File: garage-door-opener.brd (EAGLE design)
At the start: 54.3 x 47 mm, 17 parts, among them IC1 LM2575-3.3T, K1 RR1A, T1 BC547, X2 Connector

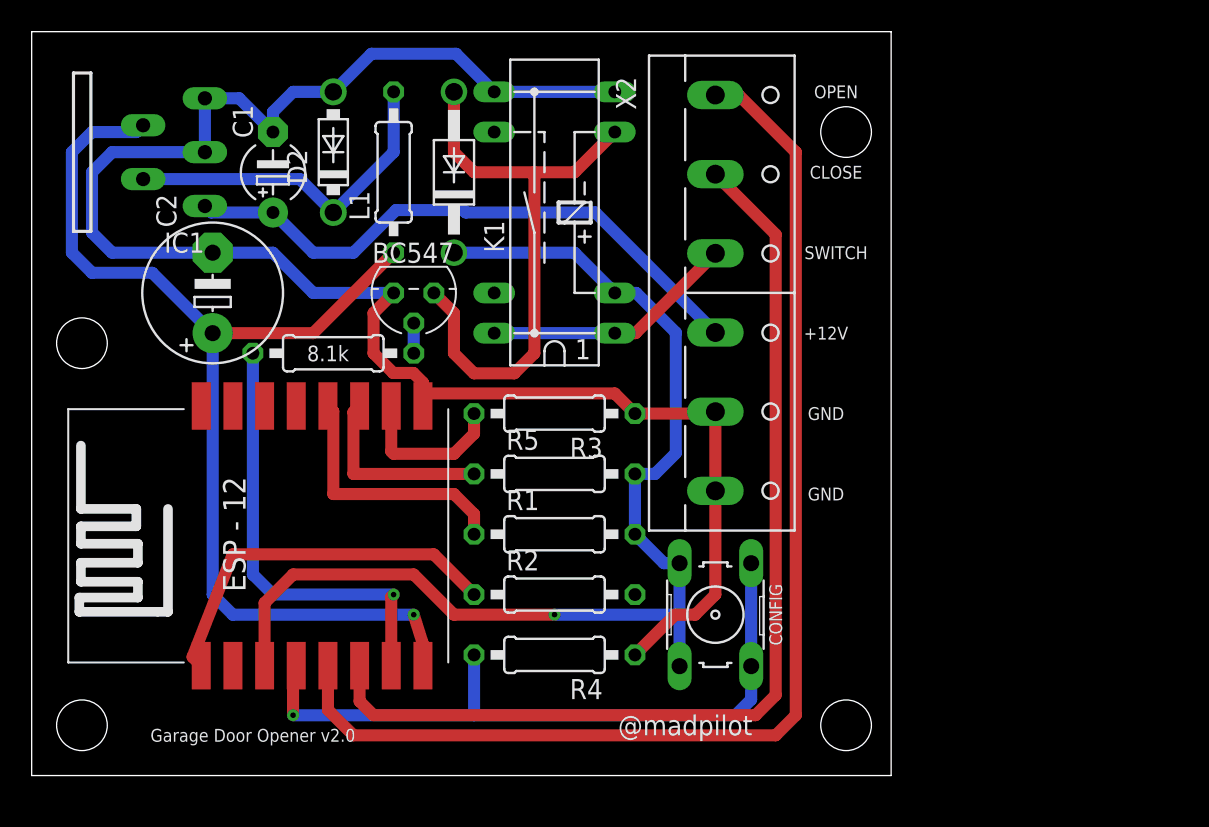
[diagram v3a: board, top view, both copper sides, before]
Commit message: Adding pogo pins to ESP8266 for prgoramming. Fixing DRC errors - still some errors with the programmer mount screws.
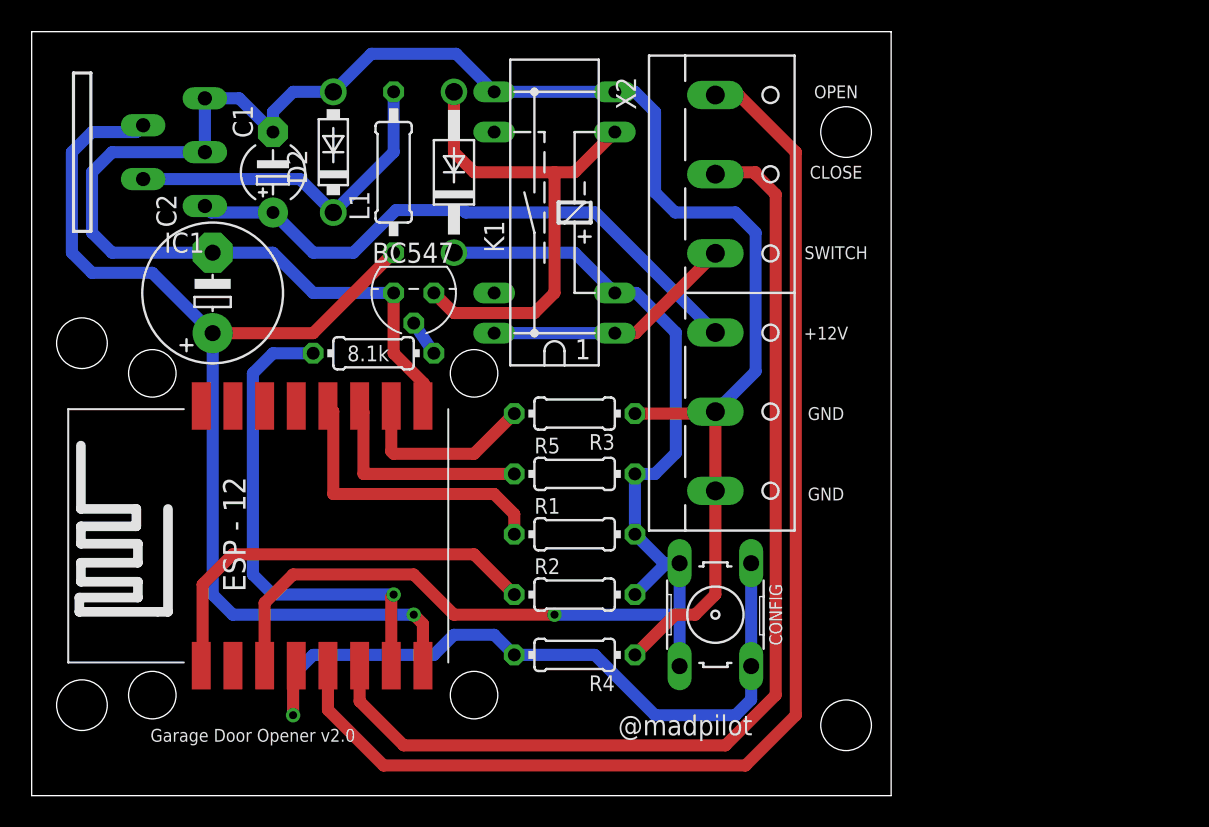
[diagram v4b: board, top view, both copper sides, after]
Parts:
- R1, R2, R3, R4, R5, R8: device resistor:0207/10 -> resistor:0204/7
- S1: value (none) -> Config
- U1: value (none) -> ESP8266; device esp8266modules:ESP12-SMD -> esp8266modules:ESP12-SMD-POGO
- moved R8 2.54 mm to (21.6, 63.5)
- moved U1 1.27 mm to (15.2, 52.1)
- moved R1 1.27 mm to (34.3, 52.1)
- moved R2 1.27 mm to (34.3, 48.3)
- moved R3 1.27 mm to (34.3, 59.7)
- moved R4 1.27 mm to (34.3, 44.5)
- moved R5 1.27 mm to (34.3, 55.9)
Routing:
- net GND: track 113.0 -> 125.2 mm
- net N$1: track 37.4 -> 31.8 mm
- net N$10: track 63.9 -> 67.1 mm
- net N$9: track 27.9 -> 31.0 mm
- net VCC: track 72.7 -> 75.4 mm
- net N$8: track 24.0 -> 26.7 mm
- net N$7: track 16.4 -> 18.9 mm
- net N$12: track 45.0 -> 46.9 mm
- net N$13: track 12.1 -> 13.9 mm
- net N$6: track 9.96 -> 11.8 mm
- net N$11: track 75.7 -> 77.2 mm
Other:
- board size 54.3 x 47 mm -> 54.3 x 48.2 mm

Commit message: Using silk screen to indicate drill hold position for programmer (you probably don't want holes in a production board). For dev boards, you just need to manually drill 4 holes
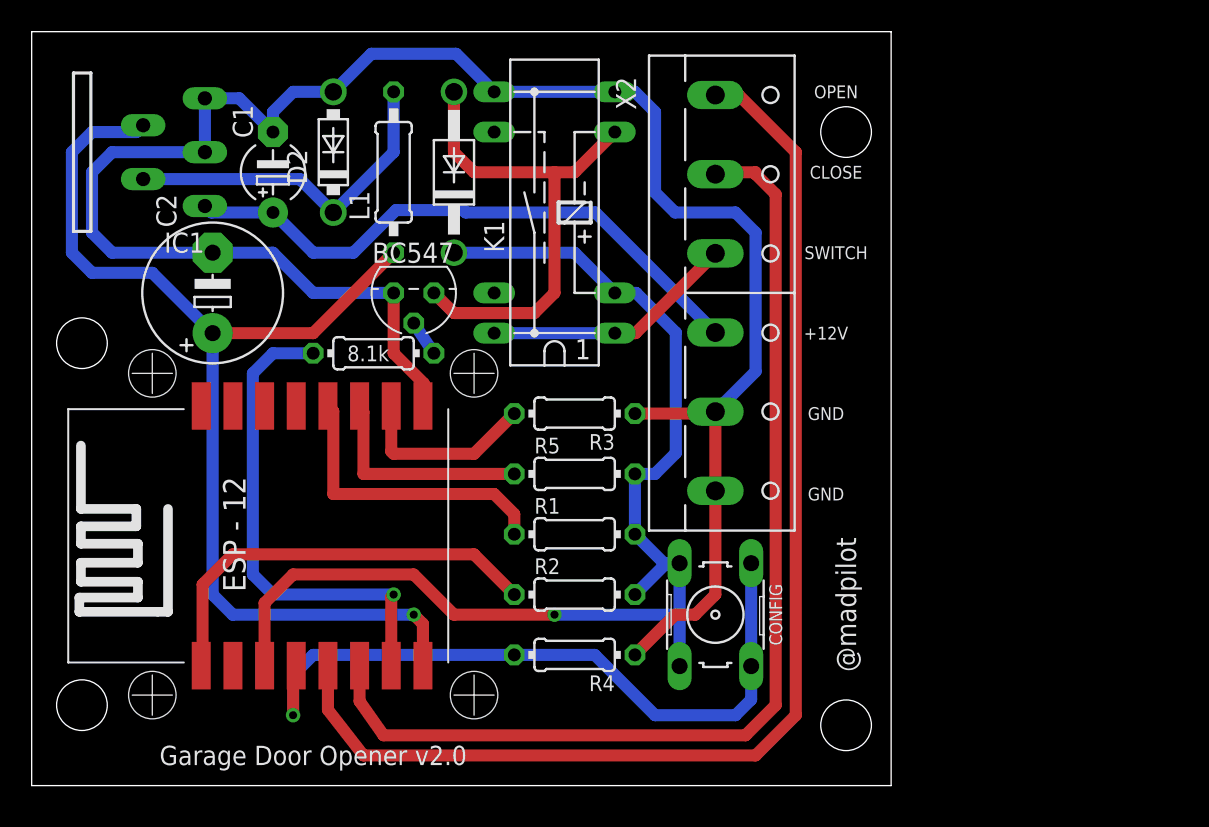
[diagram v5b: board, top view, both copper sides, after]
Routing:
- net N$12: track 46.9 -> 45.8 mm
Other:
- board size 54.3 x 48.2 mm -> 54.3 x 47.6 mm
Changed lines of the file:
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@@
 <board>
 <plain>
-<wire x1="0" y1="35.56" x2="54.28" y2="35.56" width="0" layer="20"/>
-<wire x1="54.28" y1="35.56" x2="54.28" y2="83.81" width="0" layer="20"/>
+<wire x1="0" y1="36.195" x2="54.28" y2="36.195" width="0" layer="20"/>
+<wire x1="54.28" y1="36.195" x2="54.28" y2="83.81" width="0" layer="20"/>
 <wire x1="54.28" y1="83.81" x2="0" y2="83.81" width="0" layer="20"/>
-<wire x1="0" y1="83.81" x2="0" y2="35.56" width="0" layer="20"/>
+<wire x1="0" y1="83.81" x2="0" y2="36.195" width="0" layer="20"/>
 <text x="50.165" y="64.77" size="0.8128" layer="21" font="vector" ratio="5" align="center">+12V</text>
 <text x="50.165" y="59.69" size="0.8128" layer="21" font="vector" ratio="5" align="center">GND</text>
@@
 <text x="50.8" y="74.93" size="0.8128" layer="21" ratio="5" align="center">CLOSE</text>
 <text x="50.8" y="69.85" size="0.8128" layer="21" font="vector" ratio="5" align="center">SWITCH</text>
-<text x="13.97" y="39.37" size="0.8128" layer="21" font="vector" ratio="5" align="center">Garage Door Opener v2.0</text>
-<text x="41.275" y="40.005" size="1.27" layer="21" font="vector" ratio="5" align="center">@madpilot</text>
+<text x="17.78" y="38.1" size="1.2192" layer="21" font="vector" ratio="5" align="center">Garage Door Opener v2.0</text>
+<text x="51.435" y="47.625" size="1.27" layer="21" font="vector" ratio="5" rot="R90" align="center">@madpilot</text>
 <hole x="3.175" y="41.275" drill="3.2"/>
 <hole x="3.175" y="64.135" drill="3.2"/>
@@
 <contactref element="U1" pad="GPIO12"/>
 <wire x1="20.71" y1="43.77" x2="20.71" y2="41.52" width="0.762" layer="1"/>
-<wire x1="20.71" y1="41.52" x2="23.495" y2="38.735" width="0.762" layer="1"/>
-<wire x1="23.495" y1="38.735" x2="43.815" y2="38.735" width="0.762" layer="1"/>
-<wire x1="43.815" y1="38.735" x2="46.99" y2="41.91" width="0.762" layer="1"/>
-<wire x1="46.99" y1="41.91" x2="46.99" y2="73.54" width="0.762" layer="1"/>
+<wire x1="20.71" y1="41.52" x2="22.225" y2="39.37" width="0.762" layer="1"/>
+<wire x1="22.225" y1="39.37" x2="45.085" y2="39.37" width="0.762" layer="1"/>
+<wire x1="45.085" y1="39.37" x2="46.99" y2="41.275" width="0.762" layer="1"/>
+<wire x1="46.99" y1="41.275" x2="46.99" y2="73.54" width="0.762" layer="1"/>
 <wire x1="46.99" y1="73.54" x2="45.72" y2="74.81" width="0.762" layer="1"/>
 <wire x1="45.72" y1="74.81" x2="45.72" y2="74.93" width="0.762" layer="1"/>
@@
 <contactref element="U1" pad="GPIO14"/>
 <wire x1="18.71" y1="43.77" x2="18.71" y2="40.98" width="0.762" layer="1"/>
-<wire x1="18.71" y1="40.98" x2="22.225" y2="37.465" width="0.762" layer="1"/>
-<wire x1="22.225" y1="37.465" x2="45.085" y2="37.465" width="0.762" layer="1"/>
-<wire x1="45.085" y1="37.465" x2="48.26" y2="40.64" width="0.762" layer="1"/>
+<wire x1="18.71" y1="40.98" x2="20.955" y2="38.1" width="0.762" layer="1"/>
+<wire x1="20.955" y1="38.1" x2="45.72" y2="38.1" width="0.762" layer="1"/>
+<wire x1="45.72" y1="38.1" x2="48.26" y2="40.64" width="0.762" layer="1"/>
 <wire x1="48.26" y1="76.2" x2="44.65" y2="79.81" width="0.762" layer="1"/>
 <wire x1="44.65" y1="79.81" x2="43.18" y2="79.81" width="0.762" layer="1"/>
@@
 <wire x1="17.78" y1="44.45" x2="16.51" y2="43.18" width="0.762" layer="16"/>
 <wire x1="16.51" y1="43.18" x2="16.51" y2="40.64" width="0.762" layer="16"/>
-<wire x1="30.48" y1="44.45" x2="29.21" y2="45.72" width="0.762" layer="16"/>
-<wire x1="29.21" y1="45.72" x2="26.67" y2="45.72" width="0.762" layer="16"/>
-<wire x1="26.67" y1="45.72" x2="25.4" y2="44.45" width="0.762" layer="16"/>
-<wire x1="25.4" y1="44.45" x2="17.78" y2="44.45" width="0.762" layer="16"/>
+<wire x1="30.48" y1="44.45" x2="17.78" y2="44.45" width="0.762" layer="16"/>
 </signal>
 <signal name="N$6">
